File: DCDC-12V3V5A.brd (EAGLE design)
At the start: 40 x 23 mm, 36 parts, among them CN2 2828XX-2282834-2, CN3 2828XX-2282834-2, Q10 NMOSFET, Q9 NMOSFET, U1 LM3150MHX/NOPB

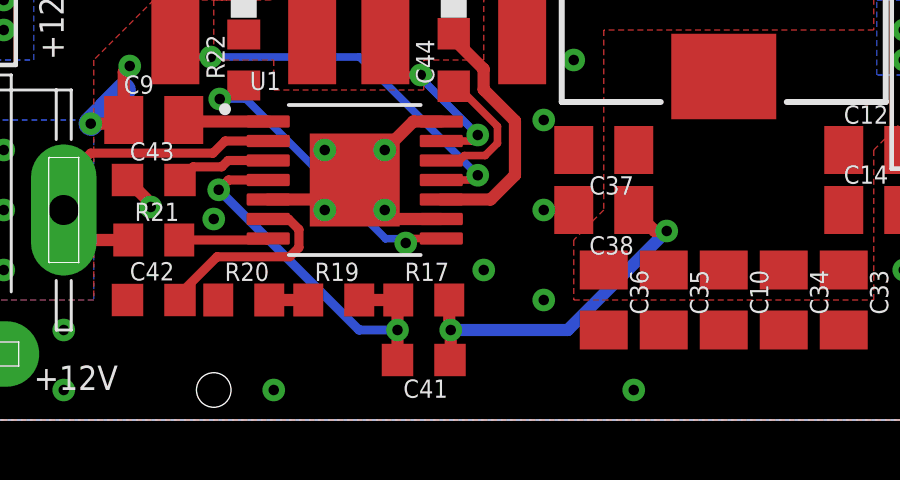
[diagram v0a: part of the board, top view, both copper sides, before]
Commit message: Fixed few values on 3.3V schematics. Generated CAM files.
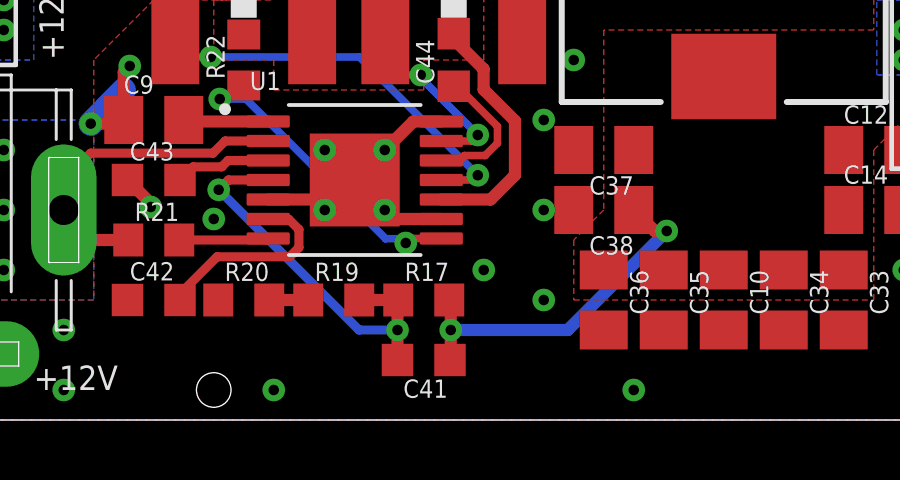
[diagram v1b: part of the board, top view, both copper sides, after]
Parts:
- C41: value 100pF -> 200pF
- R21: value 82k -> 47k
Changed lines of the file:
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@@
 <drawing>
 <settings>
-<setting alwaysvectorfont="yes"/>
+<setting alwaysvectorfont="no"/>
 <setting verticaltext="up"/>
 </settings>
@@
 <attribute name="VALUE" x="26" y="8.9" size="0.6096" layer="27" font="vector" rot="R180"/>
 </element>
-<element name="C41" library="rcl" library_urn="urn:adsk.eagle:library:334" package="C0603K" package3d_urn="urn:adsk.eagle:package:23680/2" value="100pF" x="19" y="2" smashed="yes" rot="R180">
+<element name="C41" library="rcl" library_urn="urn:adsk.eagle:library:334" package="C0603K" package3d_urn="urn:adsk.eagle:package:23680/2" value="200pF" x="19" y="2" smashed="yes" rot="R180">
 <attribute name="NAME" x="19.8" y="1.35" size="0.6096" layer="25" font="vector" rot="R180"/>
 <attribute name="POPULARITY" value="30" x="-34.34" y="57.88" size="1.778" layer="27" rot="R180" display="off"/>
@@
 <attribute name="VALUE" x="12.365" y="2.095" size="0.6096" layer="27" font="vector"/>
 </element>
-<element name="R21" library="rcl" library_urn="urn:adsk.eagle:library:334" package="R0603" package3d_urn="urn:adsk.eagle:package:23555/3" value="82k" x="10" y="6" smashed="yes">
+<element name="R21" library="rcl" library_urn="urn:adsk.eagle:library:334" package="R0603" package3d_urn="urn:adsk.eagle:package:23555/3" value="47k" x="10" y="6" smashed="yes">
 <attribute name="NAME" x="9.365" y="6.635" size="0.6096" layer="25" font="vector"/>
 <attribute name="POPULARITY" value="70" x="26.51" y="-44.8" size="1.778" layer="27" display="off"/>
@@
 <via x="35" y="12" extent="1-16" drill="0.35"/>
 <contactref element="LED1" pad="A"/>
-<wire x1="19.9" y1="3" x2="19.85" y2="3.05" width="0.4064" layer="1"/>
-<wire x1="19.85" y1="3.05" x2="19.85" y2="4" width="0.4064" layer="1"/>
+<wire x1="19.9" y1="3" x2="19.9" y2="4" width="0.4064" layer="1"/>
+<wire x1="19.85" y1="4" x2="19.9" y2="4" width="0.4064" layer="1"/>
 <wire x1="19.9" y1="3" x2="19.9" y2="2.025" width="0.4064" layer="1"/>
 <wire x1="19.9" y1="2.025" x2="19.875" y2="2" width="0.4064" layer="1"/>

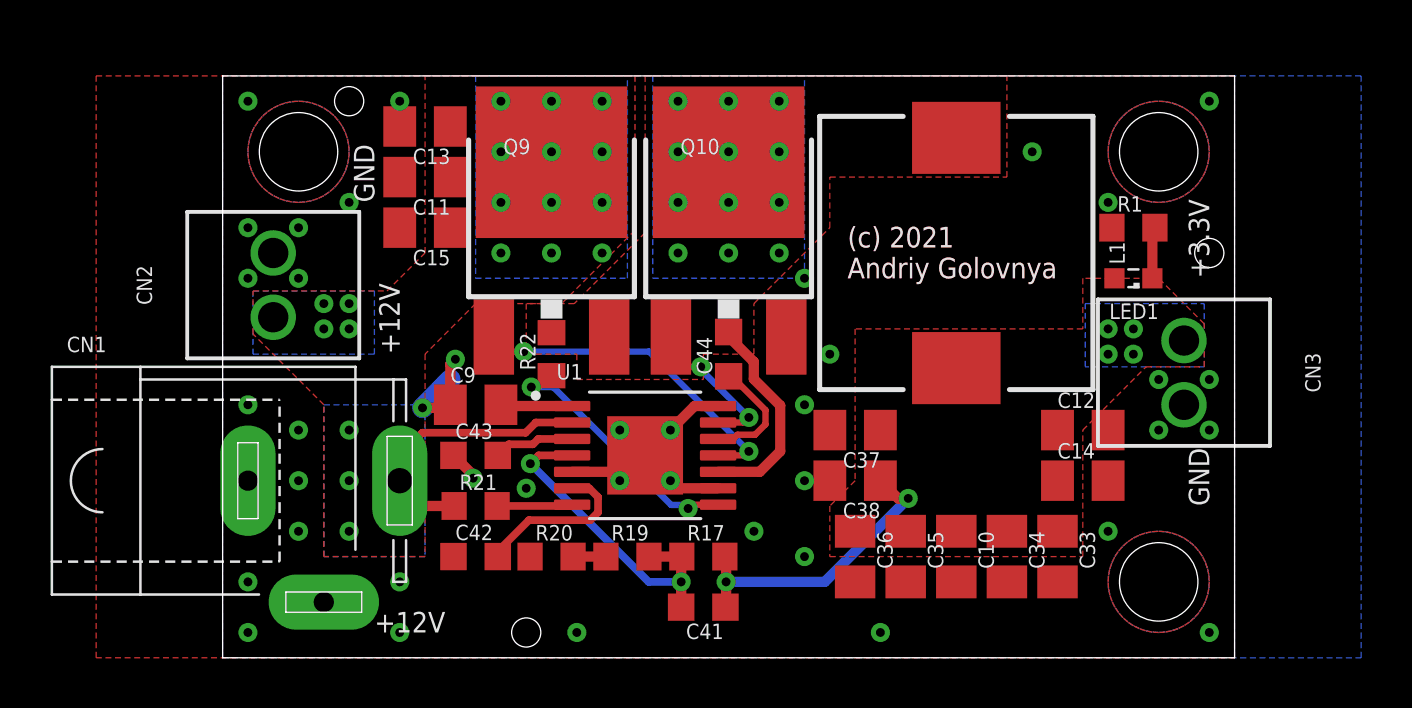
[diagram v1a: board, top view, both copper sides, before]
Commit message: Improved layout of DC-DC board. Rotated input terminal. Generated CAM files. Generated BoM and PnP files. Generated PNG preview. Generated PDF schematics.
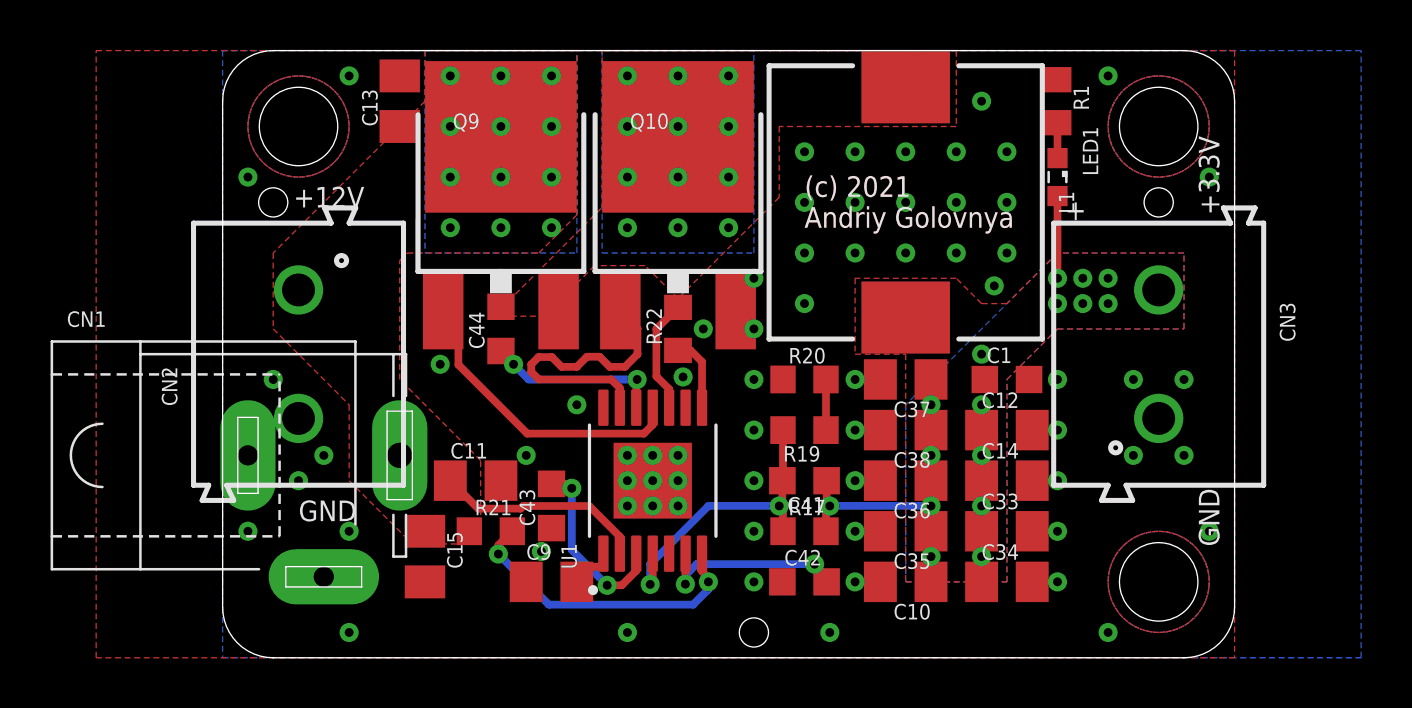
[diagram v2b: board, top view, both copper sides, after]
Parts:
- added C1: 1nF, rcl:C0603K
- CN2, CN3: value 2828XX-2282834-2 -> (none); device Connector:TERMBLK_254-2N -> Wurth_Connectors_WR-TBL Rising Cage Clamp:691213510002
- R1: value 2k -> 1k
- moved C42 13.0 mm to (23.0, 3.00)
- moved C15 13.0 mm to (8.00, 4.00), turned to 270 degrees
- moved R20 12.2 mm to (23.0, 11.0)
- moved C11 12.2 mm to (10.0, 7.00), turned to 0 degrees
- moved C44 9.06 mm to (11.0, 13.0)
- moved HOLE3 9.00 mm to (21.0, 1.00)
- moved R19 8.60 mm to (23.0, 9.00), turned to 180 degrees
- moved C9 7.62 mm to (13.0, 3.00)
- moved C41 6.40 mm to (23.0, 7.00)
- moved R1 5.83 mm to (33.0, 22.0), turned to 270 degrees
- moved R22 5.10 mm to (18.0, 13.0)
- moved HOLE2 5.00 mm to (2.00, 18.0)
- moved LED1 5.00 mm to (33.0, 19.0), turned to 270 degrees
- moved CN2 4.12 mm to (3.00, 12.0)
- moved R17 4.12 mm to (23.0, 5.00)
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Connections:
- net N$16 renamed BUCK_SS
- net N$18 renamed BUCK_EN
- net N$19 renamed BUCK_VCC
- net N$21 renamed BUCK_RON
- net N$23 renamed BUCK_BST
- net N$8 renamed BUCK_ILIM
- removed net 3.3V: C10.1, C12.1, C14.1, C33.1, C34.1, C35.1, C36.1, C37.1, C38.1, C41.1, CN3.2, L1.2, LED1.A, R17.2
- new net 5V: C1.1, C10.1, C12.1, C14.1, C33.1, C34.1, C35.1, C36.1, C37.1, C38.1, C41.1, CN3.2, L1.2, LED1.A, R17.2
- net GND: now also C1.2, CN2.2; no longer CN2.1
- net VIN: now also CN2.1; no longer CN2.2
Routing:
- net GND: track 12.1 -> 0.00 mm, vias 40 -> 69
- net 3.3V: track 12.0 -> 0.00 mm, vias 6 -> 0
- net 5V: track 0.00 -> 9.36 mm, vias 0 -> 16
- net BUCK_RON: track 2.99 -> 12.0 mm, vias 0 -> 2
- net BUCK_ILIM: track 10.4 -> 2.95 mm, vias 2 -> 0
- net BUCK_LG: track 6.23 -> 11.8 mm, vias 2 -> 0
- net BUCK_EN: track 3.21 -> 7.35 mm, vias 0 -> 2
- net BUCK_SW: track 8.35 -> 4.53 mm
- net VIN: track 10.9 -> 8.38 mm, vias 19 -> 12
- net BUCK_BST: track 4.68 -> 6.99 mm, vias 0 -> 2
- net BUCK_HG: track 13.3 -> 12.0 mm, vias 2 -> 0
- net BUCK_SS: track 6.58 -> 7.75 mm, vias 0 -> 2
- net BUCK_VCC: track 2.84 -> 1.73 mm
- net BUCK_FB: track 13.0 -> 12.2 mm
- net N$2: track 1.30 -> 2.00 mm
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- added copper zone on layer 1, net 5V
- added copper zone on layer 16, net 5V
- removed copper zone on layer 1, net 3.3V
- removed copper zone on layer 16, net 3.3V
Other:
- board size 40 x 23 mm -> 40 x 24 mm
- board text added: "+"
- board text added: "DCDC-12V3V5A-0011"
- board text removed: "DCDC-12V3V5A-0010"

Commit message: Added proper voltage symbols on 3.3v and 12v boards. Generated PDF schematics.
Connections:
- net 5V renamed 3.3V
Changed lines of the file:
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@@
 <drawing>
 <settings>
-<setting alwaysvectorfont="yes"/>
+<setting alwaysvectorfont="no"/>
 <setting verticaltext="up"/>
 </settings>
@@
 <via x="29" y="18" extent="1-16" drill="0.35"/>
 </signal>
-<signal name="5V" airwireshidden="yes">
+<signal name="3.3V" airwireshidden="yes">
 <contactref element="C34" pad="1"/>
 <contactref element="C36" pad="1"/>
@@
 <via x="30" y="12" extent="1-16" drill="0.35"/>
 <wire x1="33" y1="18.25" x2="33" y2="15" width="0.3048" layer="1"/>
+<wire x1="35" y1="15" x2="37" y2="14.54" width="0" layer="19" extent="1-1"/>
+<wire x1="35" y1="14" x2="35" y2="15" width="0" layer="19" extent="1-1"/>
+<wire x1="34" y1="15" x2="35" y2="15" width="0" layer="19" extent="1-1"/>
+<wire x1="34" y1="14" x2="35" y2="14" width="0" layer="19" extent="1-1"/>
+<wire x1="33" y1="14" x2="34" y2="14" width="0" layer="19" extent="1-1"/>
+<wire x1="33" y1="15" x2="34" y2="15" width="0" layer="19" extent="1-1"/>
+<wire x1="30" y1="12" x2="33" y2="14" width="0" layer="19" extent="1-1"/>
+<wire x1="30.125" y1="11" x2="30" y2="12" width="0" layer="19" extent="1-1"/>
+<wire x1="30" y1="10" x2="30.125" y2="11" width="0" layer="19" extent="1-1"/>
+<wire x1="30" y1="9" x2="30" y2="10" width="0" layer="19" extent="1-1"/>
+<wire x1="30" y1="8" x2="30" y2="9" width="0" layer="19" extent="1-1"/>
+<wire x1="30" y1="7" x2="30" y2="8" width="0" layer="19" extent="1-1"/>
+<wire x1="30" y1="6" x2="30" y2="7" width="0" layer="19" extent="1-1"/>
+<wire x1="30" y1="5" x2="30" y2="6" width="0" layer="19" extent="1-1"/>
+<wire x1="30" y1="4" x2="30" y2="5" width="0" layer="19" extent="1-1"/>
+<wire x1="30" y1="3" x2="30" y2="4" width="0" layer="19" extent="1-1"/>
+<wire x1="28" y1="9" x2="30" y2="9" width="0" layer="19" extent="1-1"/>
+<wire x1="28" y1="10" x2="28" y2="9" width="0" layer="19" extent="1-1"/>
+<wire x1="28" y1="11" x2="28" y2="10" width="0" layer="19" extent="1-1"/>
+<wire x1="28" y1="8" x2="28" y2="9" width="0" layer="19" extent="1-1"/>
+<wire x1="28" y1="7" x2="28" y2="8" width="0" layer="19" extent="1-1"/>
+<wire x1="28" y1="6" x2="28" y2="7" width="0" layer="19" extent="1-1"/>
+<wire x1="28" y1="5" x2="28" y2="6" width="0" layer="19" extent="1-1"/>
+<wire x1="28" y1="4" x2="28" y2="5" width="0" layer="19" extent="1-1"/>
+<wire x1="28" y1="3" x2="28" y2="4" width="0" layer="19" extent="1-1"/>
+<wire x1="27" y1="13.45" x2="28" y2="11" width="0" layer="19" extent="1-1"/>
 </signal>
 <signal name="BUCK_LG">
